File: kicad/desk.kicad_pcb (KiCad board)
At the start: 2 copper layers, 94 x 60 mm, 12 parts, among them J1 DIN harness, J2 ESP32 left, J3 ESP32 right, U1 PC817, U2 PC817

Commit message: Resistors to P7.62mm footprints; board linked and ready to route
Co-Authored-By: Claude Opus 5 <noreply@anthropic.com>
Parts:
- J2: value ESP32 left -> ESP32 DevKit V1
- J3: value ESP32 right -> ESP32 DevKit V1
- R1, R2, R3, R4, R5, R6, R7: footprint Resistor_THT:R_Axial_DIN0207_L6.3mm_D2.5mm_P10.16mm_Horizontal -> Resistor_THT:R_Axial_DIN0207_L6.3mm_D2.5mm_P7.62mm_Horizontal
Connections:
- net +5V renamed /+5V
- net BLACK_DATA renamed /BLACK_DATA
- net GND renamed /GND
- net N-DIV renamed Net-(R6-Pad2)
- J1 pad 3: WHITE_UP -> /WHITE_UP
- J1 pad 4: YELLOW_DN -> /YELLOW_DN
- J2 pad 8: GPIO25 -> /GPIO25
- J2 pad 9: GPIO26 -> /GPIO26
- J3 pad 10: GPIO16 -> /GPIO16
- R1 pad 1: N-LED1 -> /GPIO25
- R1 pad 2: GPIO25 -> Net-(R1-Pad2)
- R2 pad 1: N-LED2 -> /GPIO26
- R2 pad 2: GPIO26 -> Net-(R2-Pad2)
- R3 pad 1: WHITE_UP -> unconnected-(R3-Pad1)
- R4 pad 1: YELLOW_DN -> unconnected-(R4-Pad1)
- R5 pad 2: GPIO16 -> Net-(R5-Pad2)
- R6 pad 1: GPIO16 -> Net-(R5-Pad2)
- U1 pad 1: N-LED1 -> Net-(R1-Pad2)
- U1 pad 3: WHITE_UP -> /WHITE_UP
- U2 pad 1: N-LED2 -> Net-(R2-Pad2)
- U2 pad 3: YELLOW_DN -> /YELLOW_DN

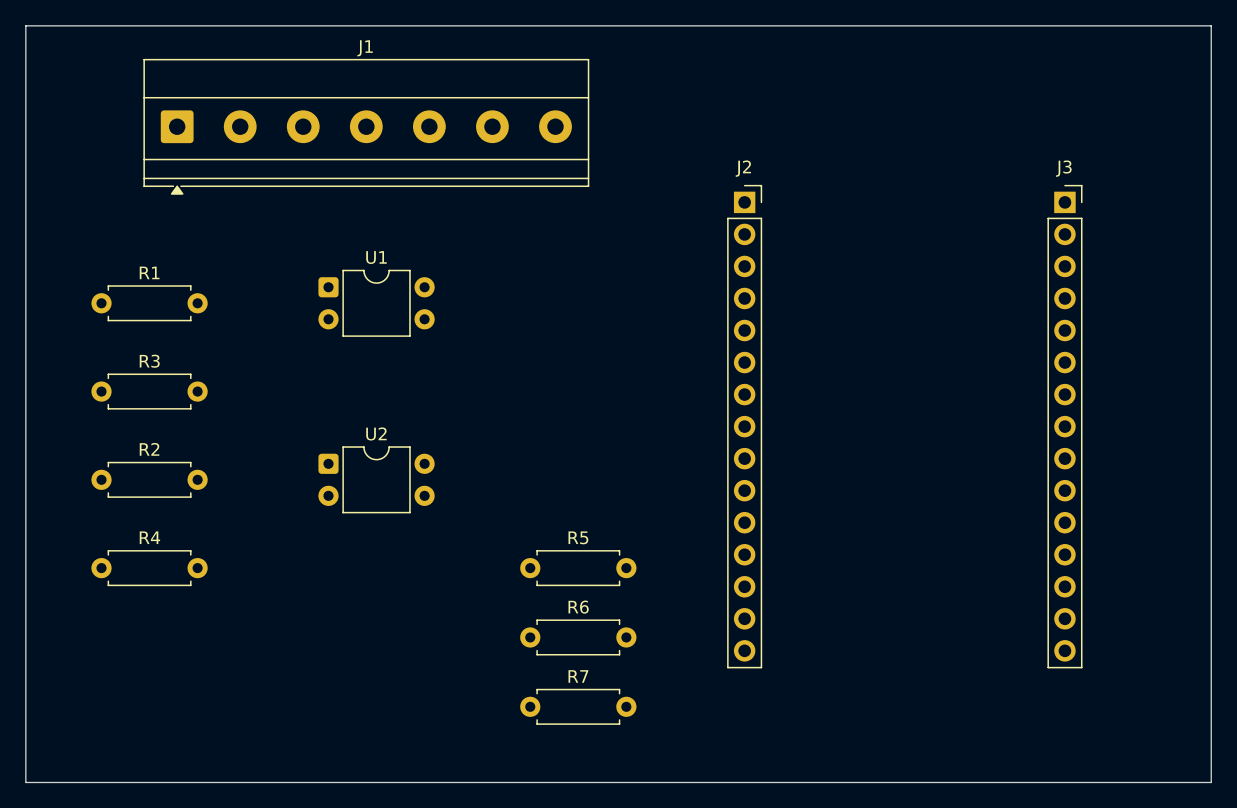
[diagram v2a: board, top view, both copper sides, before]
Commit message: Board ready to cut: J4 pass-through, GND pour, 3 mounting holes, DRC clean
Export script matches the shop guide section 4 (4.6 gerbers, X2 and netlist
attrs off, merged inch Excellon) and now emits F.Silkscreen for the laser.
Footer corrected to solve-offsets: MX/MY are per-board, and this board is
not near page origin so the geo-aux-heat constants would run it off the
fixture entirely.

Co-Authored-By: Claude Opus 5 <noreply@anthropic.com>
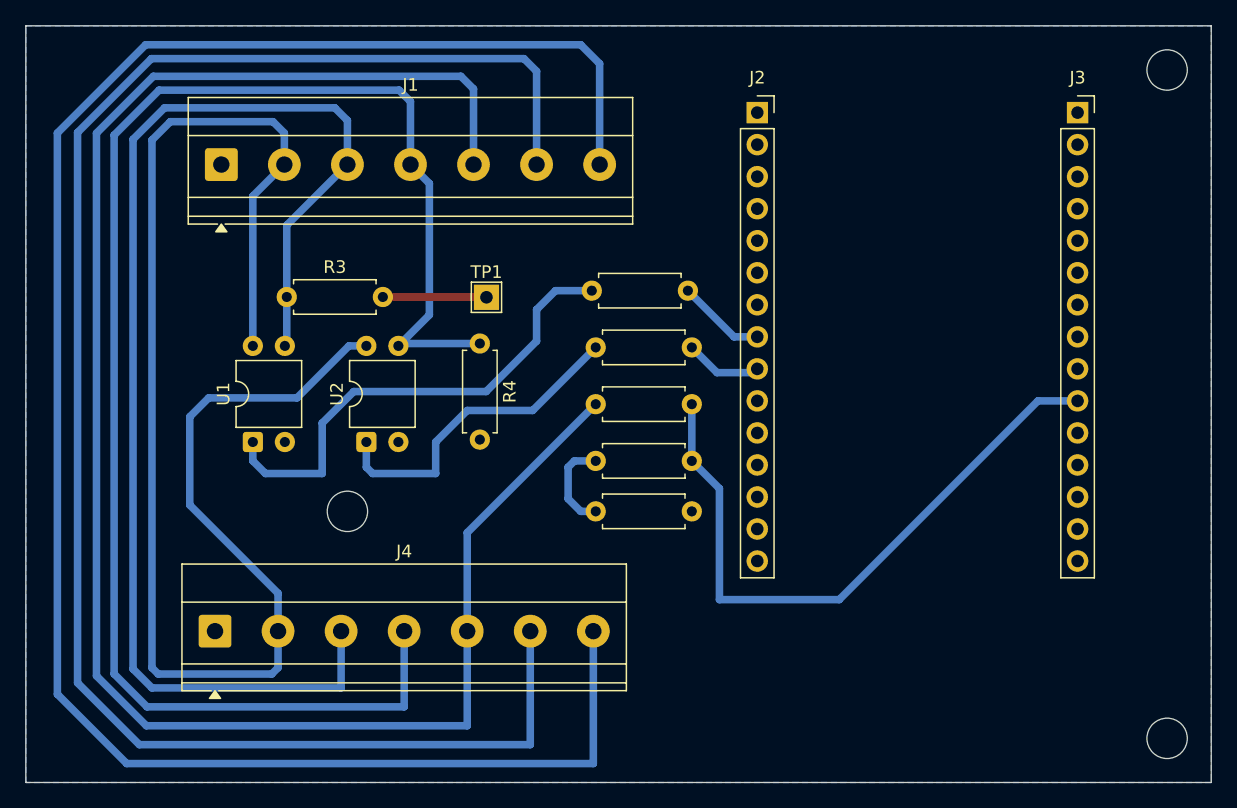
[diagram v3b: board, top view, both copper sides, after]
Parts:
- added J4: DIN harness, TerminalBlock_Phoenix:TerminalBlock_Phoenix_MKDS-1,5-7_1x07_P5.00mm_Horizontal, F.Cu at (115.0, 148.0)
- added REF**: MountingHole_3.2mm_M3, MountingHole:MountingHole_3.2mm_M3, F.Cu at (125.5, 138.5)
- added REF**: MountingHole_3.2mm_M3, MountingHole:MountingHole_3.2mm_M3, F.Cu at (190.5, 103.5)
- added REF**: MountingHole_3.2mm_M3, MountingHole:MountingHole_3.2mm_M3, F.Cu at (190.5, 156.5)
- added TP1: TestPoint_Square, TestPoint:TestPoint_Pad_2.0x2.0mm, F.Cu at (136.5, 121.5)
- moved R2 48.0 mm to (152.8, 125.5), turned to 180 degrees
- moved R1 46.5 mm to (152.5, 121.0), turned to 180 degrees
- moved R4 34.9 mm to (136.0, 125.2), turned to -90 degrees
- moved R6 19.0 mm to (152.8, 134.5), turned to 180 degrees
- moved R3 16.5 mm to (120.7, 121.5)
- moved R7 16.3 mm to (145.2, 138.5)
- moved R5 14.0 mm to (145.2, 130.0)
- moved U1 13.7 mm to (118.0, 133.0), turned to 90 degrees
- moved J2 7.19 mm to (158.0, 106.9)
- moved J3 7.19 mm to (183.4, 106.9)
- moved J1 4.61 mm to (115.5, 111.0)
- moved U2 3.46 mm to (127.0, 133.0), turned to 90 degrees
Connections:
- J1 pad 6: unconnected-(J1-Pin_6-Pad6) -> /HS3_GRN
- J1 pad 7: unconnected-(J1-Pin_7-Pad7) -> /HS4_BLUE
- R3 pad 1: unconnected-(R3-Pad1) -> /WHITE_UP
- R4 pad 1: unconnected-(R4-Pad1) -> /YELLOW_DN
- R5 pad 2: Net-(R5-Pad2) -> /GPIO16
- R6 pad 1: Net-(R5-Pad2) -> /GPIO16
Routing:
- net /HS4_BLUE: track 0.00 -> 154.3 mm
- net /BLACK_DATA: track 0.00 -> 142.0 mm
- net /HS3_GRN: track 0.00 -> 137.2 mm
- net /YELLOW_DN: track 0.00 -> 125.7 mm
- net /+5V: track 0.00 -> 120.8 mm
- net /WHITE_UP: track 0.00 -> 102.0 mm
- net /GPIO16: track 0.00 -> 51.3 mm
- net Net-(R1-Pad2): track 0.00 -> 38.6 mm
- net Net-(R2-Pad2): track 0.00 -> 26.0 mm
- net /GND: track 0.00 -> 8.19 mm
- net Net-(R6-Pad2): track 0.00 -> 7.50 mm
- net /GPIO25: track 0.00 -> 7.02 mm
- net /GPIO26: track 0.00 -> 6.14 mm
- added copper zone on B.Cu, net /GND

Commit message: Board built and running: fab pipeline, firmware fixes, build photos
Firmware: sync the public copy with the fleet version. Duty budget now
persists across reboots and credits elapsed off-time, and a diagnostic
Reset Duty Budget button is added for bench work. Fixes a stall-detection
bug where all_stop fought the seek loop at ~2 Hz, burning full duty budget
with the desk stationary. Fixes wifi.yaml.example, which nested the wifi
key and failed on first build.

KiCad: silkscreen legend, per-terminal wire-colour labels, 0.2 mm solder
mask expansion.

export_for_mill.sh: mirrored B.Mask export with mirror and geometry guards,
rasterised legend (KiCad's stroke-font SVG imports unusably), suppressed
drill circles, and a DRC gate split so warnings report without blocking.

Docs: photos of the DIN injection rig and the finished board.

Co-Authored-By: Claude Opus 5 <noreply@anthropic.com>
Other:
- rule pad_to_mask_clearance: 0 -> 0.2
- board text added: "Antenna"
- board text added: "BRN RED WHT YEL BLK GRN BLU"
- board text added: "Standing Bench V1 8/14/26 github.com/scottdube/deskhack"
